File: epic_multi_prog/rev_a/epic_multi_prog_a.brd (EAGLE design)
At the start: 48.3 x 34.3 mm, 25 parts, among them J1 EPIC-PROG-PORT, J2 MICRO_USB_B_HIROSE_ZX62R-B-5P, J3 MEC1-105-02-XX-XX-D-A, J4 TAG_CONNECT_HEADER_EPIC, U1 FT232RL, U2 MAX1555

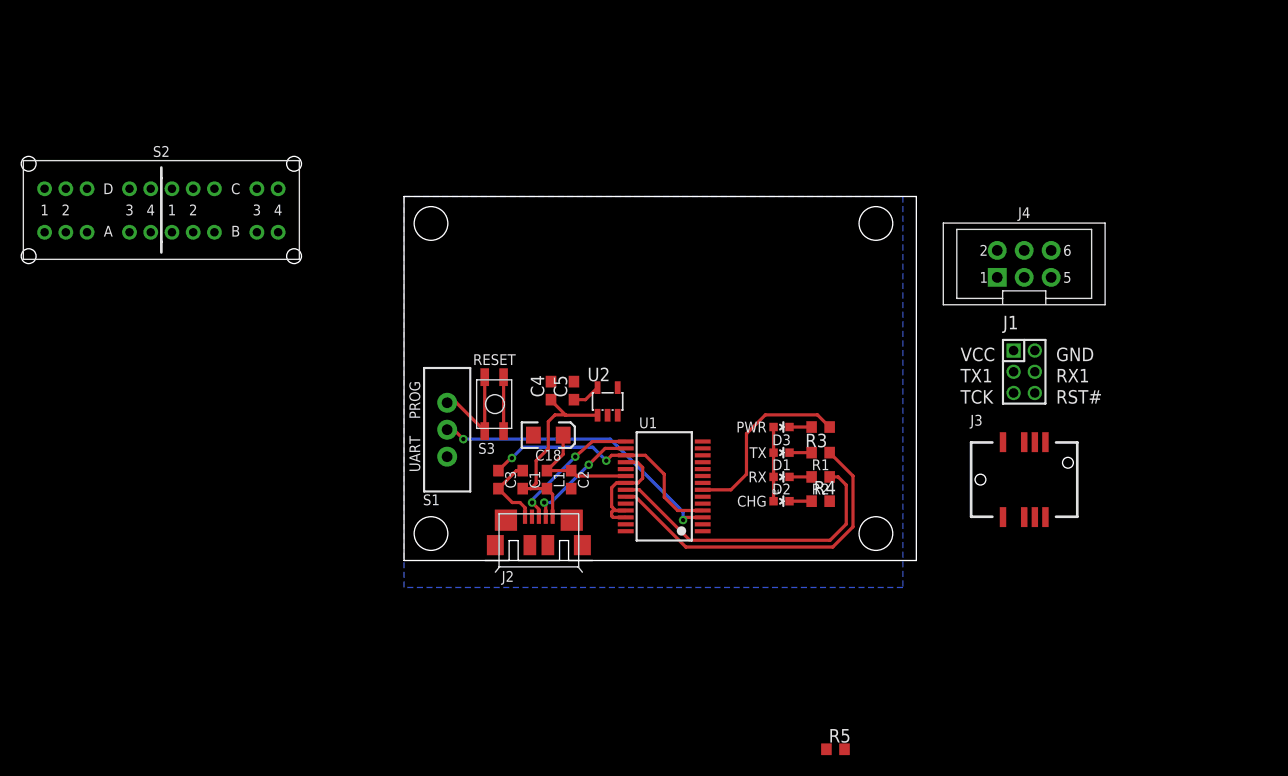
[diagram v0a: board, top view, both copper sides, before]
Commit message: Test routing to see how this board is going to look
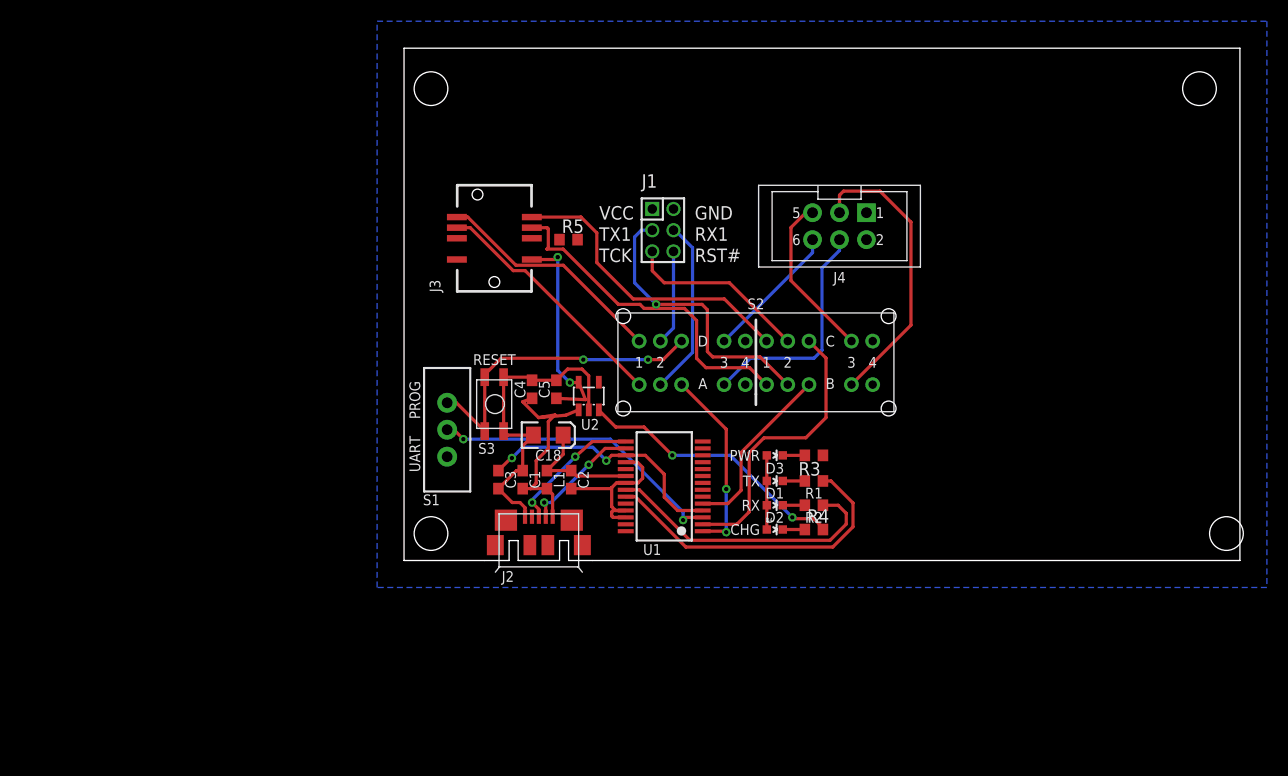
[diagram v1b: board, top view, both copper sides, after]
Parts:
- moved S2 57.8 mm to (33.1, 18.7)
- moved J3 54.8 mm to (8.51, 30.4), turned to 90 degrees
- moved R5 54.2 mm to (15.5, 30.2)
- moved J1 36.6 mm to (24.4, 31.1)
- moved J4 17.8 mm to (41.0, 31.5), turned to 180 degrees
- moved D4 2.74 mm to (34.9, 2.92)
- moved R4 2.74 mm to (38.6, 2.92)
- moved D1 2.74 mm to (34.9, 7.49)
- moved D2 2.74 mm to (34.9, 5.21)
- moved D3 2.74 mm to (34.9, 9.91)
- moved R1 2.74 mm to (38.6, 7.49)
- moved R2 2.74 mm to (38.6, 5.21)
- moved R3 2.74 mm to (38.6, 9.91)
- moved U2 1.85 mm to (17.4, 15.5)
- moved C4 1.78 mm to (12.1, 16.1)
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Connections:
- new net !RST_OPO: S2.D4
- new net RX_OPO: S2.A4
- new net TCK_OPO: S2.C4
- new net TX_OPO: S2.B4
- net !RST_EDGE: now also S2.D1
- net !RST_MINIPROG: now also S2.D2
- net !RST_POGO: now also S2.D3
- net TCK_EDGE: now also S2.C1
- net TCK_MINIPROG: now also S2.C2
- net TCK_POGO: now also S2.C3
- net TX_EDGE: now also S2.B1
- net TX_MINIPROG: now also S2.B2
- net TX_POGO: now also S2.B3
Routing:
- net TX_EDGE: track 0.00 -> 31.6 mm
- net TCK_EDGE: track 0.00 -> 28.6 mm
- net TX_POGO: track 0.00 -> 27.4 mm
- net TX_MINIPROG: track 0.00 -> 27.0 mm, vias 0 -> 1
- net TCK: track 0.00 -> 26.9 mm
- net N$12: track 0.00 -> 25.9 mm, vias 0 -> 2
- net RX_EDGE: track 0.00 -> 23.3 mm
- net !RST_EDGE: track 0.00 -> 22.0 mm
- net RX_POGO: track 0.00 -> 21.7 mm
- net !RST: track 9.72 -> 29.9 mm, vias 0 -> 2
- net RX: track 0.00 -> 17.9 mm, vias 0 -> 2
- net BATT_CHG: track 2.69 -> 20.2 mm, vias 0 -> 2
- net TCK_MINIPROG: track 0.00 -> 17.3 mm
- net TX: track 0.00 -> 16.7 mm
- net RX_MINIPROG: track 0.00 -> 16.6 mm
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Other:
- board size 48.3 x 34.3 mm -> 78.7 x 48.3 mm

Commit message: added power switches, moving things around
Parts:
- removed R5: 0 (DNP), rcl:R0603
- added S4, S5, S6: COPAL_CJS-1200TA/SPDT, switches:COPAL_CJS-1200TA/SPDT
- added SJ1: SOLDERJUMPERNO, SparkFun-Passives:SJ_2S-NO
- D1: value BLUE -> RED
- D2: value GREEN -> BLUE
- D3: value RED -> GREEN
- moved J3 49.7 mm to (54.9, 12.4)
- moved D3 4.70 mm to (34.9, 5.21)
- moved R3 4.70 mm to (38.6, 5.21)
- moved J1 3.94 mm to (20.4, 31.0)
- moved D1 2.41 mm to (34.9, 9.91)
- moved R1 2.41 mm to (38.6, 9.91)
- moved J4 2.29 mm to (38.7, 31.4)
- moved D2 2.29 mm to (34.9, 7.49)
- moved R2 2.29 mm to (38.6, 7.49)
- moved S2 0.63 mm to (33.5, 18.2)
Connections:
- new net VCC_MINIPROG: J1.P$1, S4.IN
- new net VCC_OPO: S6.IN
- new net VCC_POGO: J4.1, S5.IN
- net !RST_EDGE: now also S2.D4; no longer S2.D1
- net !RST_OPO: now also S2.D1; no longer S2.D4
- net 3V3: now also S4.2, S5.2, S6.2, SJ1.1; no longer J1.P$1, J4.1, R5.2
- net BATT_CHG: now also S4.1, S5.1, S6.1
- net GND: now also R1.1; no longer R3.1
- net N$1: now also SJ1.2; no longer R5.1
- net N$10: now also R2.1; no longer R1.1
- net N$11: now also R3.1; no longer R2.1
- net RX_EDGE: now also S2.A4; no longer S2.A1
- net RX_OPO: now also S2.A1; no longer S2.A4
- net TCK_EDGE: now also S2.C4; no longer S2.C1
- net TCK_OPO: now also S2.C1; no longer S2.C4
- net TX_EDGE: now also S2.B4; no longer S2.B1
- net TX_OPO: now also S2.B1; no longer S2.B4
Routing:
- net TX_EDGE: track 31.6 -> 0.00 mm
- net TCK_EDGE: track 28.6 -> 0.00 mm
- net RX_EDGE: track 23.3 -> 0.00 mm
- net !RST_EDGE: track 22.0 -> 0.00 mm
- net BATT_CHG: track 20.2 -> 4.51 mm, vias 2 -> 0
- net RX_MINIPROG: track 16.6 -> 20.7 mm
- net TCK_MINIPROG: track 17.3 -> 20.4 mm
- net TX_MINIPROG: track 27.0 -> 29.5 mm
- net N$11: track 26.9 -> 25.2 mm
- net TCK_POGO: track 15.7 -> 17.3 mm
- net RX_POGO: track 21.7 -> 23.2 mm
- net !RST_POGO: track 13.0 -> 14.4 mm
- net N$10: track 30.1 -> 28.8 mm
- net !RST_MINIPROG: track 8.96 -> 10.0 mm
- net RX: track 17.9 -> 17.3 mm
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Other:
- board size 78.7 x 48.3 mm -> 61 x 35.6 mm

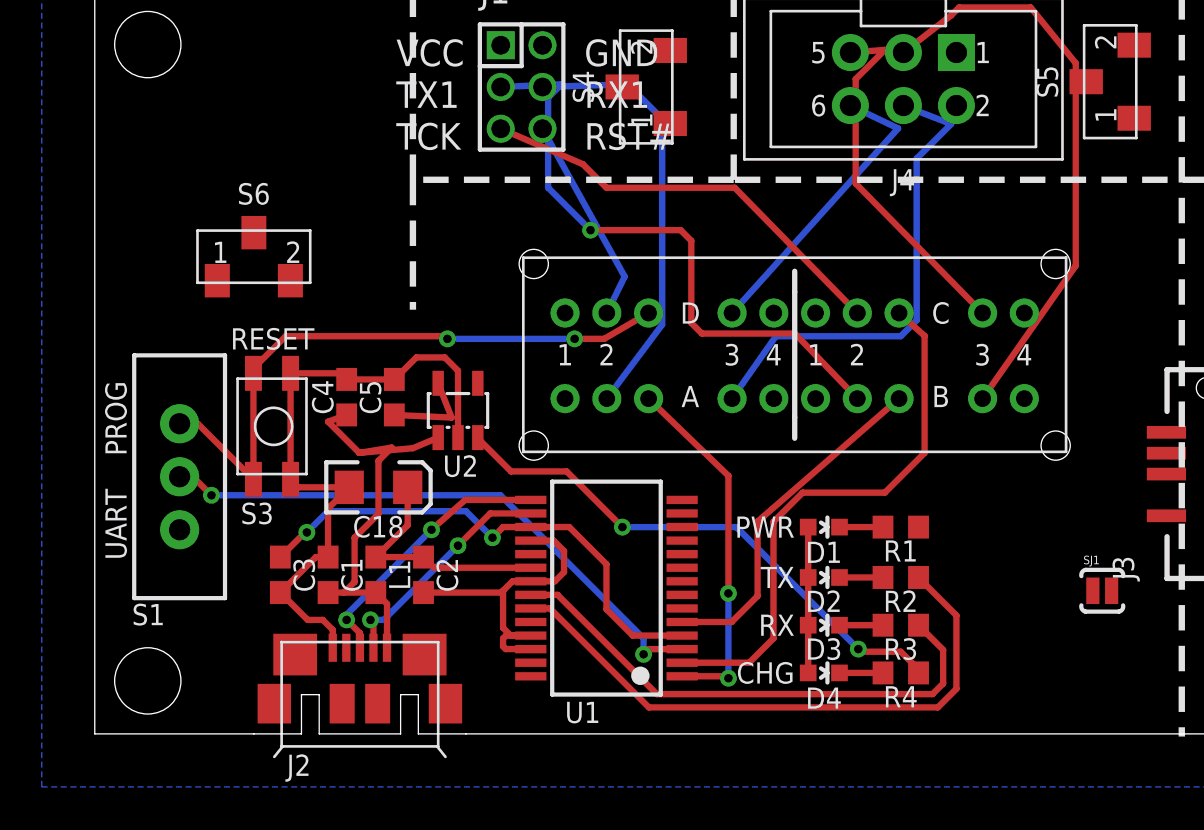
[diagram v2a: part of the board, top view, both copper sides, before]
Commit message: Moved uart/prog switch
Planning on the huge smd micro usb
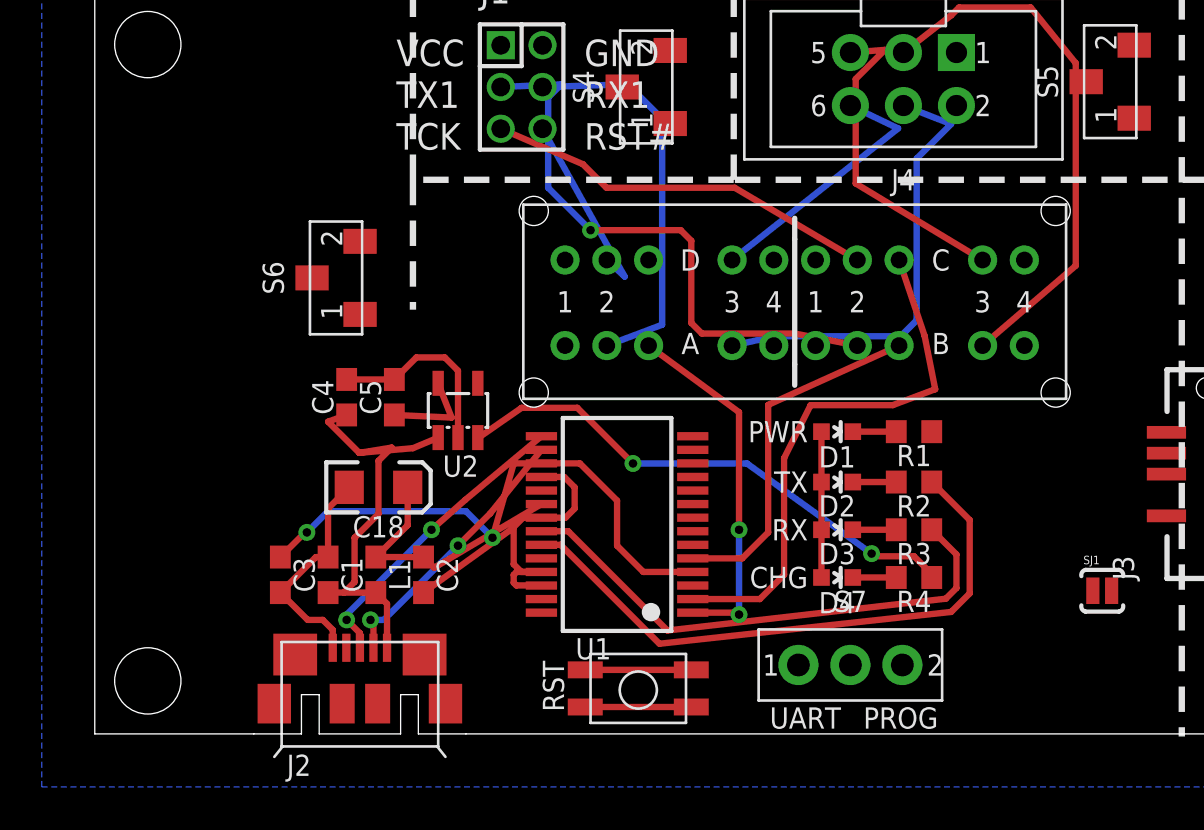
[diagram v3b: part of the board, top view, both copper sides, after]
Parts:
- removed S1: (no value), SparkFun:SWITCH-SPDT
- added S7: TE_SSA12/SPDT, switches:TE_SSA12/SPDT
- moved S3 21.6 mm to (26.0, 2.16), turned to 0 degrees
- moved D4 4.62 mm to (35.6, 7.49)
- moved R4 4.62 mm to (39.2, 7.49)
- moved D3 4.62 mm to (35.6, 9.78)
- moved R3 4.62 mm to (39.2, 9.78)
- moved D1 4.62 mm to (35.6, 14.5)
- moved D2 4.62 mm to (35.6, 12.1)
- moved R1 4.62 mm to (39.2, 14.5)
- moved R2 4.62 mm to (39.2, 12.1)
- moved S6 4.07 mm to (11.6, 21.8), turned to 90 degrees
- moved U1 3.09 mm to (25.0, 10.0)
- moved S2 2.54 mm to (33.5, 20.7)
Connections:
- new net N$13: S7.1
- net !RST: now also S7.2; no longer S1.1
- net !RST_USB: now also S7.IN; no longer S1.2
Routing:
- net !RST_USB: track 28.1 -> 0.00 mm, vias 2 -> 0
- net !RST: track 29.9 -> 5.08 mm, vias 2 -> 0
- net GND: track 47.3 -> 43.4 mm
- net 3V3: track 31.3 -> 34.3 mm
- net N$3: track 11.2 -> 13.2 mm
- net TX_POGO: track 27.8 -> 25.9 mm
- net !RST_POGO: track 14.4 -> 12.7 mm
- net N$4: track 12.9 -> 14.5 mm
- net RX_MINIPROG: track 20.7 -> 19.1 mm
- net TCK_POGO: track 17.3 -> 15.7 mm
- net TCK_MINIPROG: track 20.4 -> 18.8 mm
- net RX_POGO: track 23.2 -> 21.7 mm
- net N$6: track 11.6 -> 13.0 mm
- net TX_MINIPROG: track 29.5 -> 28.2 mm
- net !RST_MINIPROG: track 10.0 -> 9.27 mm
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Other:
- board text added: "RST"
- board text removed: "RESET"

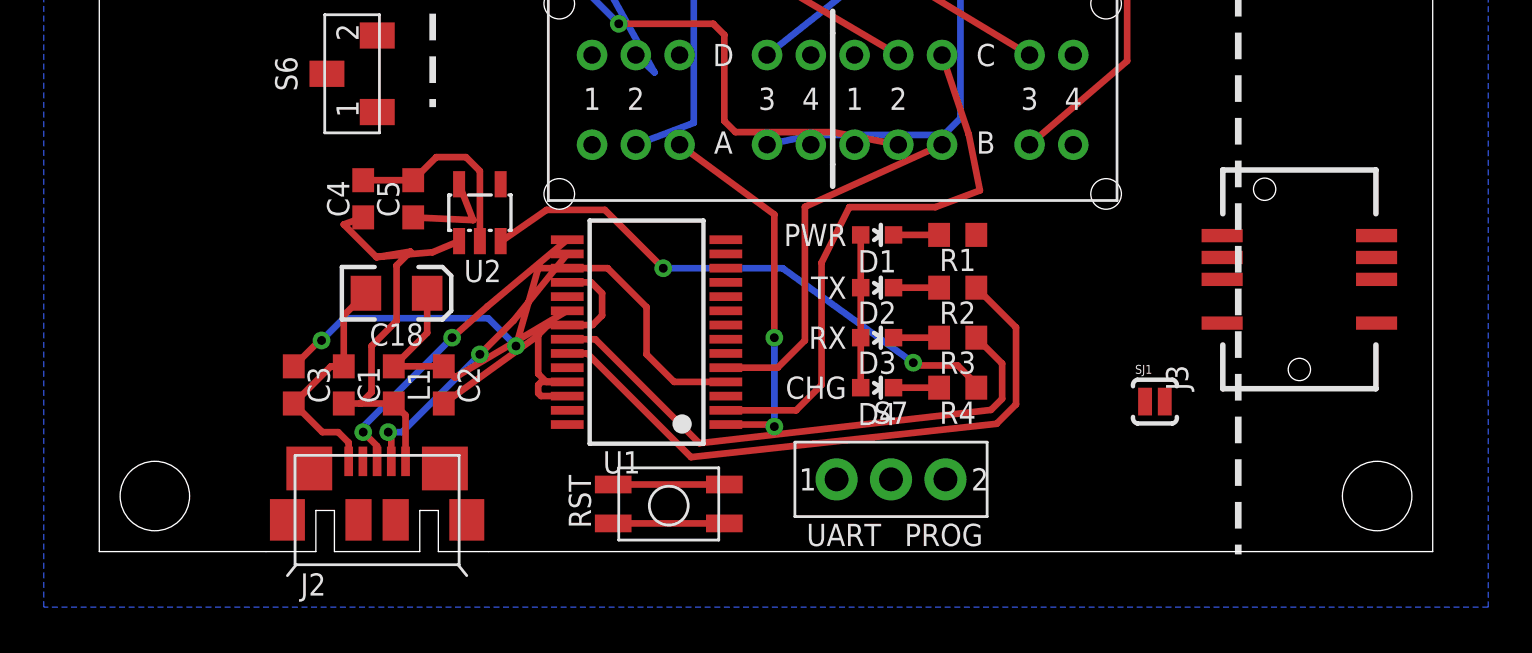
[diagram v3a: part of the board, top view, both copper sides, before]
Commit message: Moved ftdi circuit over to fill space
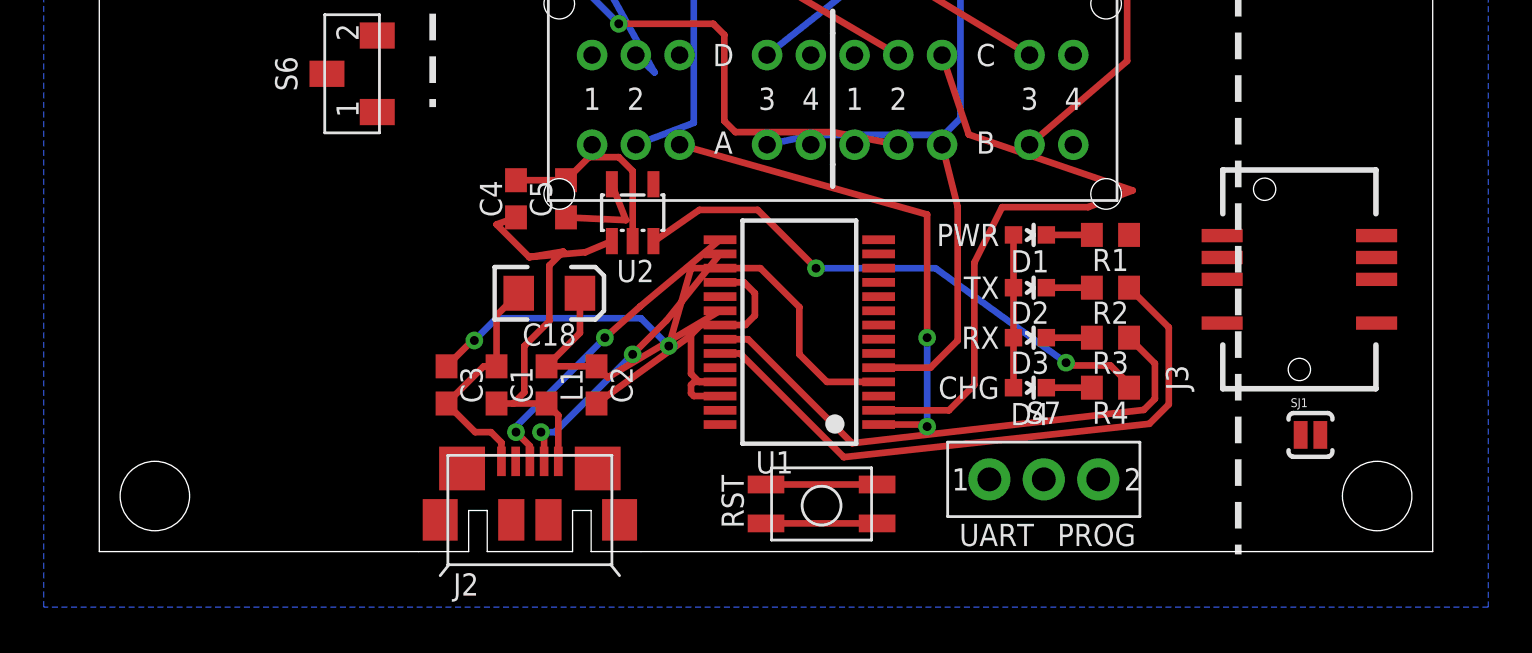
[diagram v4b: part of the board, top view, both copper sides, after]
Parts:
- moved SJ1 7.27 mm to (55.4, 5.33)
- moved S3 6.99 mm to (33.0, 2.16)
- moved C1 6.99 mm to (18.2, 7.62)
- moved C18 6.99 mm to (20.6, 11.8)
- moved C2 6.99 mm to (22.7, 7.62)
- moved C4 6.99 mm to (19.1, 16.1)
- moved C3 6.98 mm to (15.9, 7.62)
- moved D1 6.98 mm to (42.5, 14.5)
- moved D2 6.98 mm to (42.5, 12.1)
- moved D3 6.98 mm to (42.5, 9.78)
- moved D4 6.98 mm to (42.5, 7.49)
- moved J2 6.98 mm to (19.7, 0.00)
- moved L1 6.98 mm to (20.4, 7.62)
- moved R1 6.98 mm to (46.2, 14.5)
- moved R2 6.98 mm to (46.2, 12.1)
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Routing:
- net RX: track 17.3 -> 23.7 mm
- net TCK: track 25.8 -> 31.1 mm
- net TX: track 17.1 -> 13.2 mm
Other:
- outline, holes or cut-outs redrawn
